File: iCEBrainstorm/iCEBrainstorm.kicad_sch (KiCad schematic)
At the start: 136 parts, among them J1 Connector, USB-TYPE-C-16P, J10 Conn_01x02_Pin, J11 Conn_01x06_Pin, J12 Connector, USB-TYPE-C-16P, J2 Conn_01x06_Pin, J3 Conn_01x16_Pin, J4 Conn_01x08_Pin, J5 Conn_01x08_Pin, J6 Conn_01x03_Pin, J7 Conn_01x03_Pin, J8 Conn_01x02_Pin, J9 Conn_01x02_Pin, Q1 HL2312, SW1 SW_DIP_x08, SW2 SW_DIP_x08, U1 AMS1117-3.3, U2 AMS1117-1.2, U3 STM32F412RETx, U4 ICE40UP5K-SG48ITR, U5 W25Q128, X1 16 MHz

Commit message: lets push
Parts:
- removed R17: 68Ω, PCM_JLCPCB:R_0603, symbol PCM_JLCPCB-Resistors:0603,68Ω
- added R27: 68Ω, PCM_JLCPCB:R_0603, symbol PCM_JLCPCB-Resistors:0603,68Ω
- renumbered R18 to R17, R19 to R18, R20 to R19, R21 to R20, R22 to R21, R23 to R22, R24 to R23, R25 to R24, R26 to R25, R27 to R26
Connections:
- net FPGA_USB_D-: now also R25.2, R27.1
- net FUD-: now also R27.2; no longer R25.2

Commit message: cleared up a bit
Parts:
- removed D10, D11, D12, D9: Green, PCM_JLCPCB:D_0805, symbol PCM_JLCPCB-Diodes:LED,0805,Green
- removed J4, J5: Conn_01x08_Pin, Connector_PinHeader_2.54mm:PinHeader_1x08_P2.54mm_Vertical, symbol Connector:Conn_01x08_Pin
- removed JP12, JP13, JP6, JP7: SolderJumper_2_Open, Jumper:SolderJumper-2_P1.3mm_Open_RoundedPad1.0x1.5mm, symbol Jumper:SolderJumper_2_Open
- removed R21, R22, R23, R24: 15kΩ, PCM_JLCPCB:R_0603, symbol PCM_JLCPCB-Resistors:0603,15kΩ
- removed R35, R36, R37, R38: 1.5kΩ, PCM_JLCPCB:R_0603, symbol PCM_JLCPCB-Resistors:0603,1.5kΩ
- removed SW2: SW_DIP_x08, Button_Switch_THT:SW_DIP_SPSTx08_Slide_6.7x21.88mm_W7.62mm_P2.54mm_LowProfile, symbol Switch:SW_DIP_x08
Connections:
- net IN_GND1 is gone; now on net IN1: SW1.6
- net LED_GND1 is gone; now on net IN3: SW1.8
- net +3V3: now also SW1.10, SW1.11, SW1.12, SW1.9
- net GND: now also R17.1, R18.1, R19.1, R20.1, R31.2, R32.2, R33.2, R34.2; no longer SW1.10, SW1.11, SW1.12, SW1.9
- net IN0: now also SW1.5; no longer U3.14 (PA0)
- net IN1: no longer U3.15 (PA1)
- net IN2: now also SW1.7; no longer U3.56 (PB4)
- net IN3: no longer U3.62 (PB9)
- net IN4: no longer names the net of U4.10 (IOB_18a)
- net IN5: no longer names the net of U4.11 (IOB_20a)
- net IN6: no longer names the net of U4.6 (IOB_13b)
- net IN7: no longer names the net of U4.4 (IOB_8a)
- removed net IN_GND0: R17.1, R18.1, R19.1, R20.1, SW1.5
- removed net LED_GND0: R31.2, R32.2, R33.2, R34.2, SW1.7
- net OUT4: no longer names the net of U4.46 (IOB_0a)
- net OUT5: no longer names the net of U4.45 (IOB_5b)
- net OUT6: no longer names the net of U4.43 (IOT_49a)
- net OUT7: no longer names the net of U4.42 (IOT_51a)
- net OUT8 renamed OUT_STM
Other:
- moved on the sheet: D13, R39

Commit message: gekocht mit luci
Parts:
- added C33, C34: 100nF, PCM_JLCPCB:C_0603, symbol PCM_JLCPCB-Capacitors:0603,100nF
- added R21, R22, R23, R24: 1.5kΩ, PCM_JLCPCB:R_0603, symbol PCM_JLCPCB-Resistors:0603,1.5kΩ
- added U6: LSM6DS3, Package_LGA:LGA-14_3x2.5mm_P0.5mm_LayoutBorder3x4y, symbol Sensor_Motion:LSM6DS3
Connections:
- net +3V3: now also C33.1, C34.1, U6.5 (VDDIO), U6.8 (VDD)
- net GND: now also C33.2, C34.2, R21.2, R22.2, R23.2, R24.2, U6.6 (GND), U6.7 (GND)
- net I2C1_SCL: now also U6.13 (SCL)
- net I2C1_SDA: now also U6.14 (SDA)
- net SPI2_MISO: now also U4.6 (IOB_13b); no longer U4.31 (IOT_42b)
- net SPI2_MOSI: now also U4.4 (IOB_8a); no longer U4.28 (IOT_41a)
- net SPI2_NSS: now also U4.11 (IOB_20a); no longer U4.34 (IOT_44b)
- net SPI2_SCK: now also U4.10 (IOB_18a); no longer U4.32 (IOT_43a)
- net FPGA_BUS0: no longer names the net of U3.50 (PA15)
- net FPGA_BUS0: no longer U4.23 (IOT_37a)
- net FPGA_BUS1: no longer names the net of U3.54 (PD2)
- net FPGA_BUS1: no longer U4.25 (IOT_36b)
- new net: R22.1, U6.3 (SCX)
- new net: R23.1, U6.2 (SDX)
- new net: R24.1, U6.1 (SDO/SA0)
- new net: R21.1, U6.12 (CS)
- no-connect marks 16 -> 18
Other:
- note added: "Accelero & Gyro"
- note added: "SW1 OFF: Custom Boot SW1 ON: STM Bootloader SW2 OFF: System Memory (default) SW2 ON: Embedded SRAM Boot SW3 OFF: FPGA Custom Boot SW3 ON: FPGA USB DFU Programmer SW4 OFF: FPGA Boot from Flash SW4 ON: FPGA Boot from SPI SW[5:8]: INPUT"
- note removed: "SW1 OFF: Custom Boot SW1 ON: STM Bootloader SW2 OFF: System Memory (default) SW2 ON: Embedded SRAM Boot SW3 OFF: FPGA Custom Boot SW3 ON: FPGA USB DFU Programmer SW4 OFF: FPGA Boot from Flash SW4 ON: FPGA Boot from SPI SW5 OFF: Enable IN0 SW5 ON: Disable IN0 SW6 OFF: Enable IN1 SW6 ON: Disable IN1 SW7 OFF: Enable OUT0 SW7 ON: Disable OUT0 SW8 OFF: Enable OUT1 SW8 ON: Disable OUT1"

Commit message: wider mit luci gekocht
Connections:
- net IN3 is gone; now on net FPGA_GLOBAL_1: R20.2, SW1.8
- net +3V3: no longer J3.10 (Pin_10)
- net BTN0: now also U4.31 (IOT_42b); no longer U4.36 (IOT_48b)
- net BTN1: now also U4.32 (IOT_43a); no longer U4.38 (IOT_50b)
- net FPGA_CLK: now also U4.20 (IOB_25b_G3); no longer U3.29 (PB10), U4.35 (IOT_46b_G0)
- net FPGA_GLOBAL_6: now also R25.1, R26.1; no longer J8.2 (Pin_2)
- net FUD+: now also U4.48 (IOB_4a); no longer U4.21 (IOB_23b)
- net FUD-: now also U4.45 (IOB_5b); no longer U4.13 (IOB_24a)
- net IN0: now also U4.34 (IOT_44b)
- net IN2: now also U4.36 (IOT_48b)
- net OUT0: now also U4.25 (IOT_36b); no longer U4.3 (IOB_9b)
- net OUT1: now also U4.26 (IOT_39a); no longer U4.2 (IOB_6a)
- net OUT2: now also U4.27 (IOT_38b); no longer U4.48 (IOB_4a)
- net OUT3: now also U4.28 (IOT_41a); no longer U4.47 (IOB_2a)
- net PC0: now also J3.11 (Pin_11); no longer J3.1 (Pin_1)
- net PC1: now also J3.12 (Pin_12); no longer J3.2 (Pin_2)
- net PC10: now also J3.2 (Pin_2); no longer J3.11 (Pin_11)
- net PC11: now also J3.3 (Pin_3); no longer J3.12 (Pin_12)
- net PC12: now also J3.4 (Pin_4); no longer J3.13 (Pin_13)
- net PC13: now also J3.8 (Pin_8); no longer J3.14 (Pin_14)
- net PC14: now also J3.9 (Pin_9); no longer J3.15 (Pin_15)
- net PC15: now also J3.10 (Pin_10); no longer J3.16 (Pin_16)
- net PC2: now also J3.13 (Pin_13); no longer J3.3 (Pin_3)
- net PC3: now also J3.14 (Pin_14); no longer J3.4 (Pin_4)
- net USART1_RX: now also U4.2 (IOB_6a); no longer U4.26 (IOT_39a)
- net USART1_TX: now also U4.3 (IOB_9b); no longer U4.27 (IOT_38b)
- net PA0: now reaches U3.14 (PA0)
- net PA0: now also J3.15 (Pin_15)
- net PA1: now reaches U3.15 (PA1)
- net PA1: now also J3.16 (Pin_16)
- net PA15: now reaches U3.50 (PA15)
- net PA15: now also J3.1 (Pin_1)
- net PD2: now reaches U3.54 (PD2)
- net PD2: now also J3.5 (Pin_5)
- net PB4: now reaches U3.56 (PB4)
- net PB4: now also J3.6 (Pin_6)
- net PB9: now reaches U3.62 (PB9)
- net PB9: now also J3.7 (Pin_7)
- net FPGA_GLOBAL_3: no longer names the net of J8.1 (Pin_1)
- net FPGA_GLOBAL_3: no longer U4.20 (IOB_25b_G3)
- net IN1 renamed FPGA_GLOBAL_0
- net FPGA_GLOBAL_0: now also U3.29 (PB10), U4.35 (IOT_46b_G0)
- net PC4: no longer names the net of U3.24 (PC4)
- net PC4: no longer J3.5 (Pin_5)
- net PC5: no longer names the net of U3.25 (PC5)
- net PC5: no longer J3.6 (Pin_6)
- net PC6: no longer names the net of U3.37 (PC6)
- net PC6: no longer J3.7 (Pin_7)
- net PC7: no longer names the net of U3.38 (PC7)
- net PC7: no longer J3.8 (Pin_8)
- net PC8: no longer names the net of U3.39 (PC8)
- net PC8: no longer J3.9 (Pin_9)
- now unconnected: U4.12 (IOB_22a)
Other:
- moved on the sheet: J3, R25, R26, R27, R28

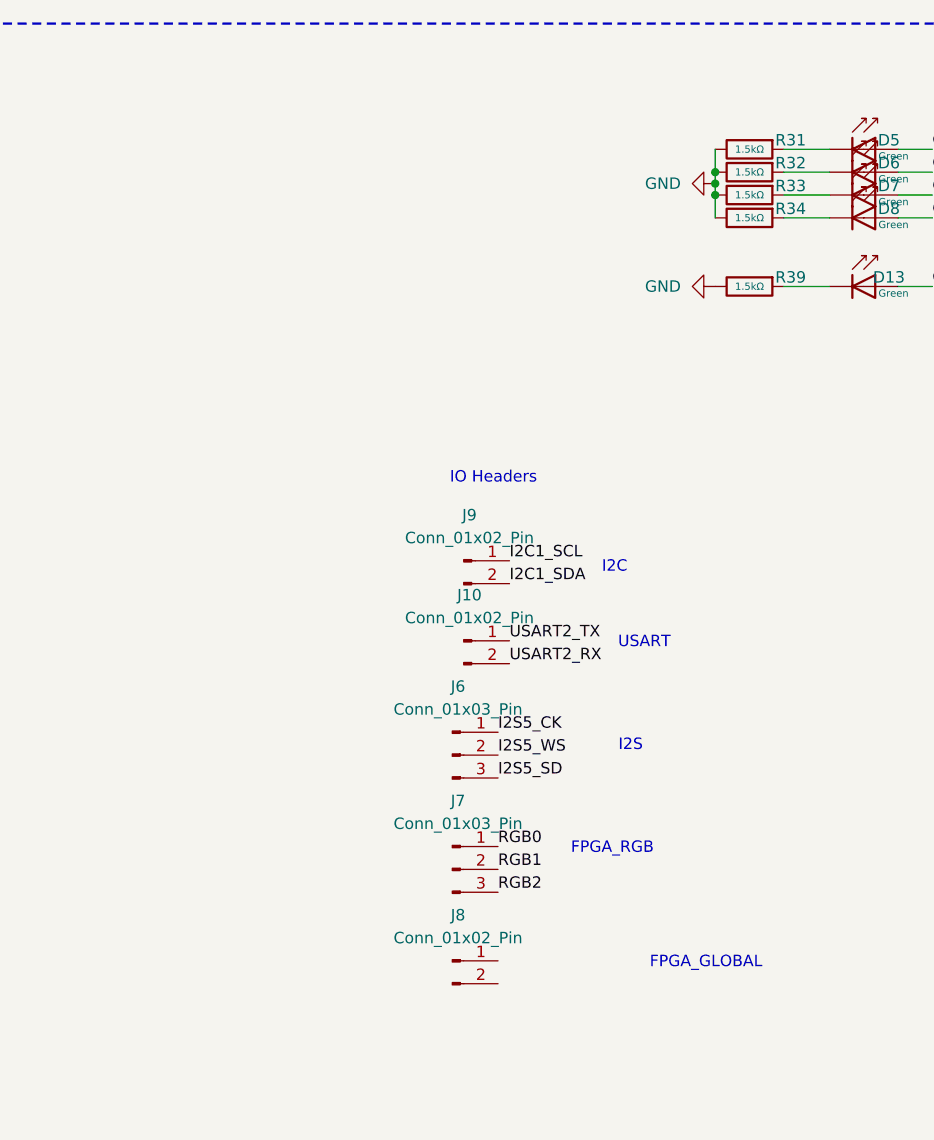
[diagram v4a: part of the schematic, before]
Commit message: did some lines + added a IN connector :)
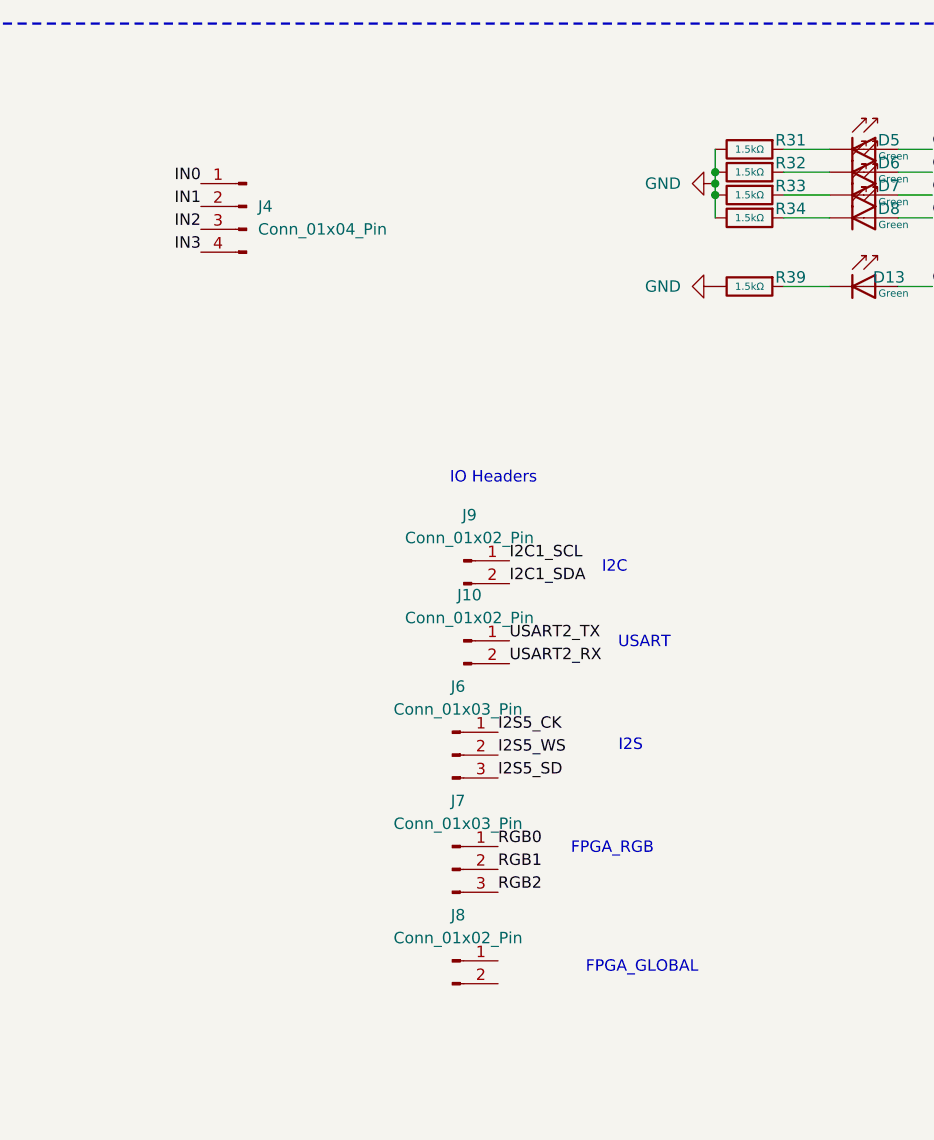
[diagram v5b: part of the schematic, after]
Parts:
- added J4: Conn_01x04_Pin, Connector_PinHeader_2.54mm:PinHeader_1x04_P2.54mm_Vertical, symbol Connector:Conn_01x04_Pin
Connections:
- net FPGA_GLOBAL_0: now also J4.2 (Pin_2)
- net FPGA_GLOBAL_1: now also J4.4 (Pin_4)
- net IN0: now also J4.1 (Pin_1)
- net IN2: now also J4.3 (Pin_3)
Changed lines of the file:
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@@
 	(text "FPGA_GLOBAL"
 		(exclude_from_sim no)
-		(at 339.344 316.484 0)
+		(at 332.232 316.992 0)
 		(effects
 			(font
@@
 		)
 	)
+	(label "IN0"
+		(at 283.21 229.87 180)
+		(effects
+			(font
+				(size 1.27 1.27)
+			)
+			(justify right bottom)
+		)
+	)
 	(label "BOOT1"
 		(at 171.45 359.41 180)
@@
 		)
 	)
+	(label "IN1"
+		(at 283.21 232.41 180)
+		(effects
+			(font
+				(size 1.27 1.27)
+			)
+			(justify right bottom)
+		)
+	)
 	(label "OUT0"
 		(at 308.61 64.77 180)
@@
 		)
 	)
+	(label "IN2"
+		(at 283.21 234.95 180)
+		(effects
+			(font
+				(size 1.27 1.27)
+			)
+			(justify right bottom)
+		)
+	)
 	(label "RGB0"
 		(at 316.23 303.53 0)
@@
 		)
 	)
+	(label "IN3"
+		(at 283.21 237.49 180)
+		(effects
+			(font
+				(size 1.27 1.27)
+			)
+			(justify right bottom)
+		)
+	)
 	(label "FPGA_SPI_SO"
 		(at 392.43 167.64 180)
@@
 					(unit 1)
 				)
+			)
+		)
+	)
+	(symbol
+		(lib_id "Connector:Conn_01x04_Pin")
+		(at 288.29 232.41 0)
+		(mirror y)
+		(unit 1)
+		(exclude_from_sim no)
+		(in_bom yes)
+		(on_board yes)
+		(dnp no)
+		(fields_autoplaced yes)
+		(property "Reference" "J4"
+			(at 289.56 232.4099 0)
+			(effects
+				(font
+					(size 1.27 1.27)
+				)
+				(justify right)
+			)
+		)
+		(property "Value" "Conn_01x04_Pin"
+			(at 289.56 234.9499 0)
+			(effects
+				(font
+					(size 1.27 1.27)
+				)
+				(justify right)
+			)
+		)
+		(property "Footprint" "Connector_PinHeader_2.54mm:PinHeader_1x04_P2.54mm_Vertical"
+			(at 288.29 232.41 0)
+			(effects
+				(font
+					(size 1.27 1.27)
+				)
+				(hide yes)
+			)
+		)
+		(property "Datasheet" "~"
+			(at 288.29 232.41 0)
+			(effects
+				(font
+					(size 1.27 1.27)
+				)
+				(hide yes)
+			)
+		)
+		(property "Description" "Generic connector, single row, 01x04, script generated"
+			(at 288.29 232.41 0)
+			(effects
+				(font
+					(size 1.27 1.27)
+				)
+				(hide yes)
+			)
+		)
+		(pin "3"
+		)
+		(pin "1"
+		)
+		(pin "4"
+		)
+		(pin "2"
+		)
+		(instances
+			(project ""
+				(path "/a979115e-05e2-465d-a941-b2ab44135948"
+					(reference "J4")
+					(unit 1)
+				)

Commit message: added uart1 connector, added power connectors, added schema back silkscreen symbol
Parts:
- added J13, J14, J15, J5: Conn_01x02_Pin, Connector_PinHeader_2.54mm:PinHeader_1x02_P2.54mm_Vertical, symbol Connector:Conn_01x02_Pin
- added N1: Housing, iCE-Brain Silkscreen, JJ:iCE-Brain, symbol Mechanical:Housing
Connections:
- net +3V3: now also J13.1 (Pin_1), J14.1 (Pin_1), J15.1 (Pin_1)
- net GND: now also J13.2 (Pin_2), J14.2 (Pin_2), J15.2 (Pin_2)
- net USART1_RX: now also J5.2 (Pin_2)
- net USART1_TX: now also J5.1 (Pin_1)
- net FPGA_BUS0: now reaches U4.12 (IOB_22a)
- net FPGA_BUS0: now also U3.25 (PC5)
- net FPGA_BUS1: now reaches U4.13 (IOB_24a)
- net FPGA_BUS1: now also U3.24 (PC4)
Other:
- note added: "POWER"
- note added: "TODO: change UART1 to something else. We need UART1 to programm the stm"
- note added: "USART1"
- note added: "USART2"
- note removed: "USART"

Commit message: did some routing
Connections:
- net FPGA_GLOBAL_1: no longer U3.41 (PA8)
- net FPGA_GLOBAL_6: now also U3.41 (PA8)
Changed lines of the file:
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@@
 	)
 	(rectangle
-		(start 251.46 212.09)
-		(end 454.66 406.4)
+		(start 48.26 212.09)
+		(end 251.46 406.4)
 		(stroke
 			(width 0.254)
@@
 		)
 	)
-	(label "FPGA_GLOBAL_1"
-		(at 185.42 82.55 0)
-		(effects
-			(font
-				(size 1.27 1.27)
-			)
-			(justify left bottom)
-		)
-	)
 	(label "PC10"
 		(at 105.41 87.63 0)
@@
 		(effects
 			(font
+				(size 1.27 1.27)
+			)
+			(justify left bottom)
+		)
+	)
+	(label "FPGA_GLOBAL_6"
+		(at 185.42 82.55 0)
+		(effects
+			(font

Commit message: fertig
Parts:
- removed J8: Conn_01x02_Pin, Connector_PinHeader_2.54mm:PinHeader_1x02_P2.54mm_Vertical, symbol Connector:Conn_01x02_Pin
- added J11, J8: Conn_01x04_Pin, Connector_PinHeader_2.54mm:PinHeader_1x04_P2.54mm_Vertical, symbol Connector:Conn_01x04_Pin
- renumbered D13 to D9, J7 to J10, J9 to J12, J10 to J13, J5 to J14, J11 to J15, J12 to J16, J3 to J2, J2 to J3, J13 to J4, J14 to J5, J15 to J6, J4 to J7, J6 to J9, JP8 to JP6, JP9 to JP7, JP10 to JP8, JP11 to JP9, R17 to R11, R18 to R12, R19 to R13, R20 to R14, R11 to R15, R12 to R16, R13 to R17, R14 to R18, R15 to R19, R16 to R20, R29 to R21, R30 to R22, R31 to R23, R32 to R24, R33 to R25, R34 to R26, R39 to R27, R40 to R28, R41 to R29, R42 to R30, R43 to R31, R44 to R32, R45 to R33, R24 to R34, R23 to R35, R22 to R36, R46 to R37, R47 to R38, R25 to R39, R26 to R40, R21 to R41, R27 to R42, R28 to R43
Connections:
- net FPGA_GLOBAL_0: no longer U3.29 (PB10)
- net FPGA_GLOBAL_6: no longer R39.1, R40.1
- net OUT0: now also J8.1 (Pin_1)
- net OUT1: now also J8.2 (Pin_2)
- net OUT2: now also J8.3 (Pin_3)
- net OUT3: now also J8.4 (Pin_4)
- net FPGA_IO_0: now reaches U4.47 (IOB_2a)
- net FPGA_IO_0: now also J11.1 (Pin_1)
- net FPGA_IO_3: now reaches U4.23 (IOT_37a)
- net FPGA_IO_3: now also J11.4 (Pin_4)
- net FPGA_IO_2: now reaches U4.38 (IOT_50b)
- net FPGA_IO_2: now also J11.3 (Pin_3)
- net FPGA_IO_1: now reaches U4.42 (IOT_51a)
- net FPGA_IO_1: now also J11.2 (Pin_2)
- net FUPP: now reaches U4.43 (IOT_49a)
- net FUPP: now also R39.1, R40.1
- no-connect marks 18 -> 24
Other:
- note added: "FPGA_IO"
- note removed: "FPGA_GLOBAL"
- moved on the sheet: J7
